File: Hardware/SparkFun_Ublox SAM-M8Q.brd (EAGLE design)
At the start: 40.6 x 40.6 mm, 74 parts, among them J13 Qwiic Right Angle, J3 PTH, J4 Qwiic Right Angle, U2 SAM-M8Q

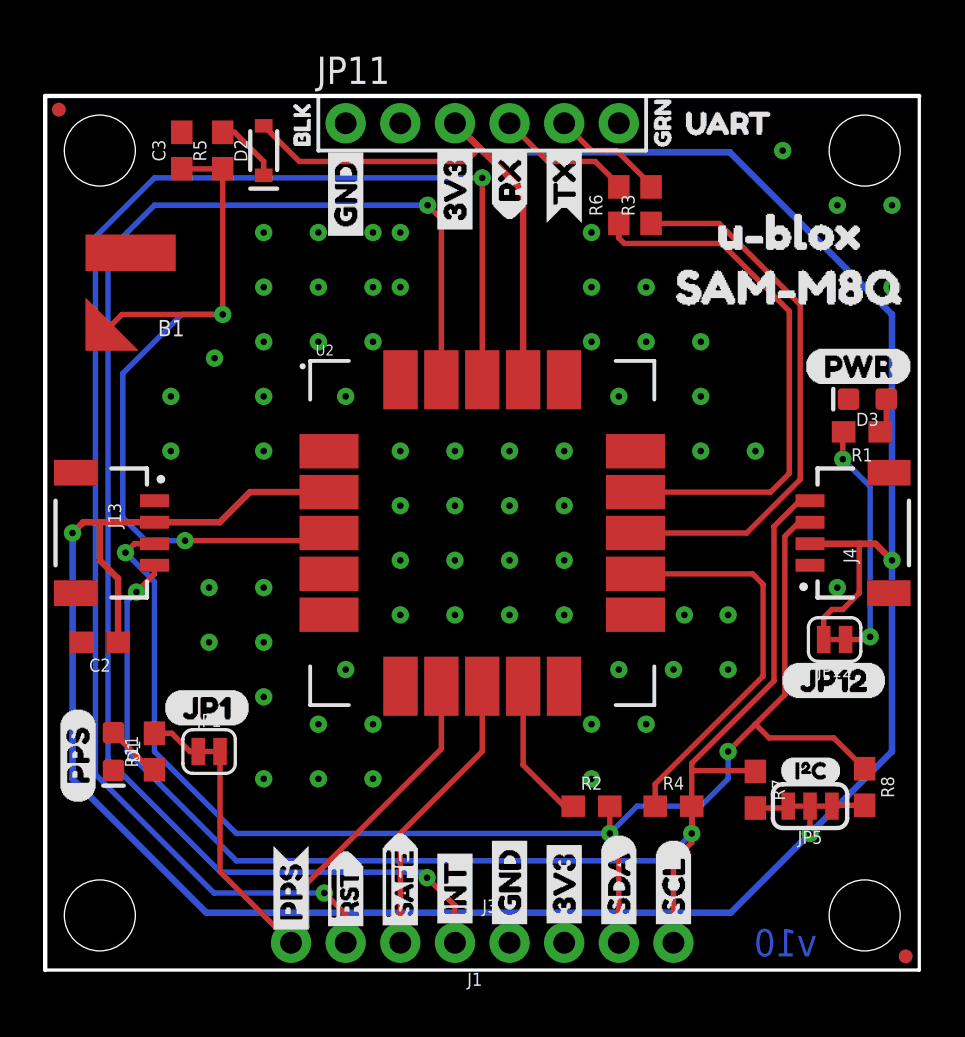
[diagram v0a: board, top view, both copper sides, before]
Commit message: Replaces all part with SparkFun parts, moves temp libarary parts to SparkFun Eagle libararies
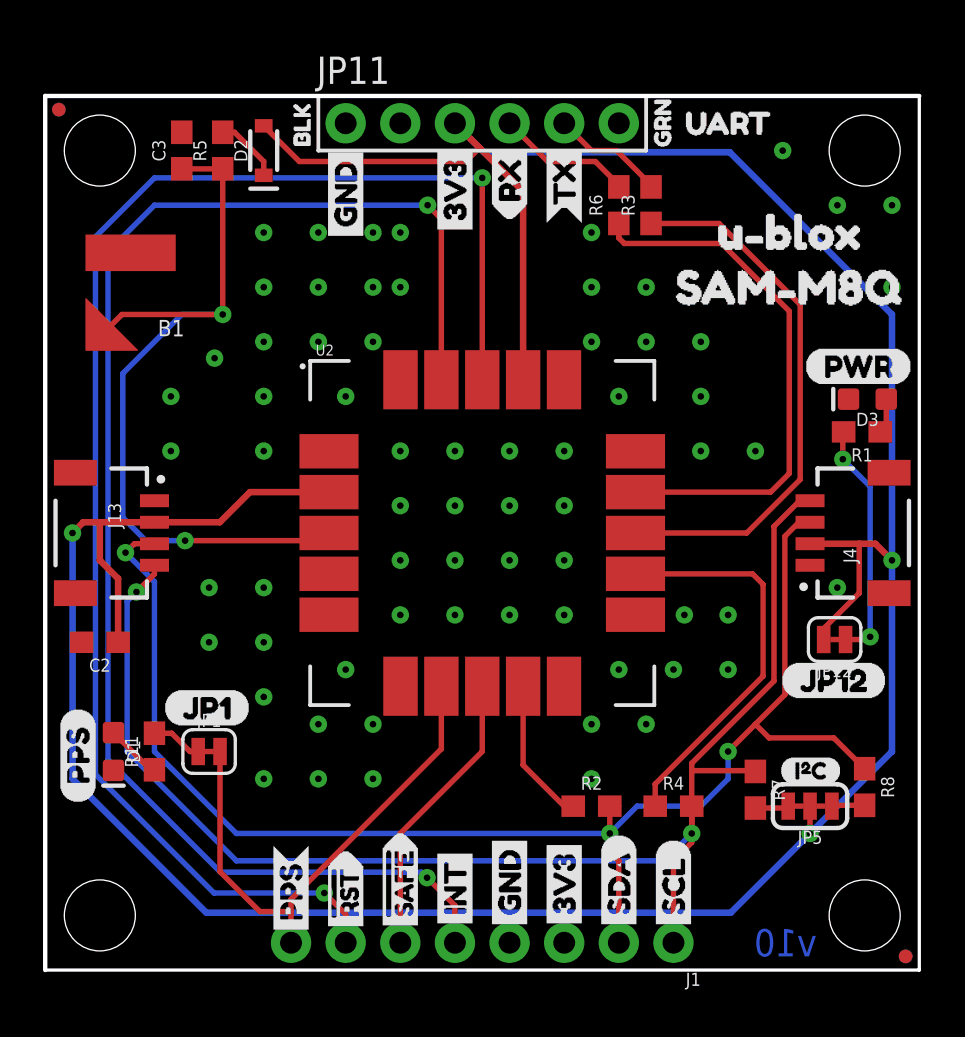
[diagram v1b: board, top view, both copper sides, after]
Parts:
- removed J3: PTH, SparkX:1X04_NO_SILK
- J1: device SparkFun-Connectors:1X04_NO_SILK -> SparkFun-Connectors:1X08_NO_SILK
- JP10, JP3, JP4, JP9: device SparkFun:STAND-OFF -> SparkFun-Hardware:STAND-OFF
- JP2, JP6, JP7, JP8: device SparkFun:MICRO-FIDUCIAL -> SparkFun-Aesthetics:FIDUCIAL-MICRO
- U2: value SAM-M8Q -> UBLOX_SAM-M8Q; device SAM-M8Q:SAM-M8Q -> SparkFun-GPS:SAM-M8Q
- moved J1 10.2 mm to (29.2, 1.27)
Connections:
- net !RESET: now also J1.7; no longer J1.3
- net !SAFE: now also J1.6; no longer J1.2
- net 3.3V: now also J1.3; no longer J3.2
- net GND: now also J1.4; no longer J3.1
- net INT: now also J1.5; no longer J1.1
- net PPS: now also J1.8; no longer J1.4
- net SCL: now also J1.1; no longer J3.4
- net SDA: now also J1.2; no longer J3.3
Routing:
- net PPS: track 25.1 -> 24.5 mm

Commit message: Changes all drill sizes to 15 mil, adjust schematic labels
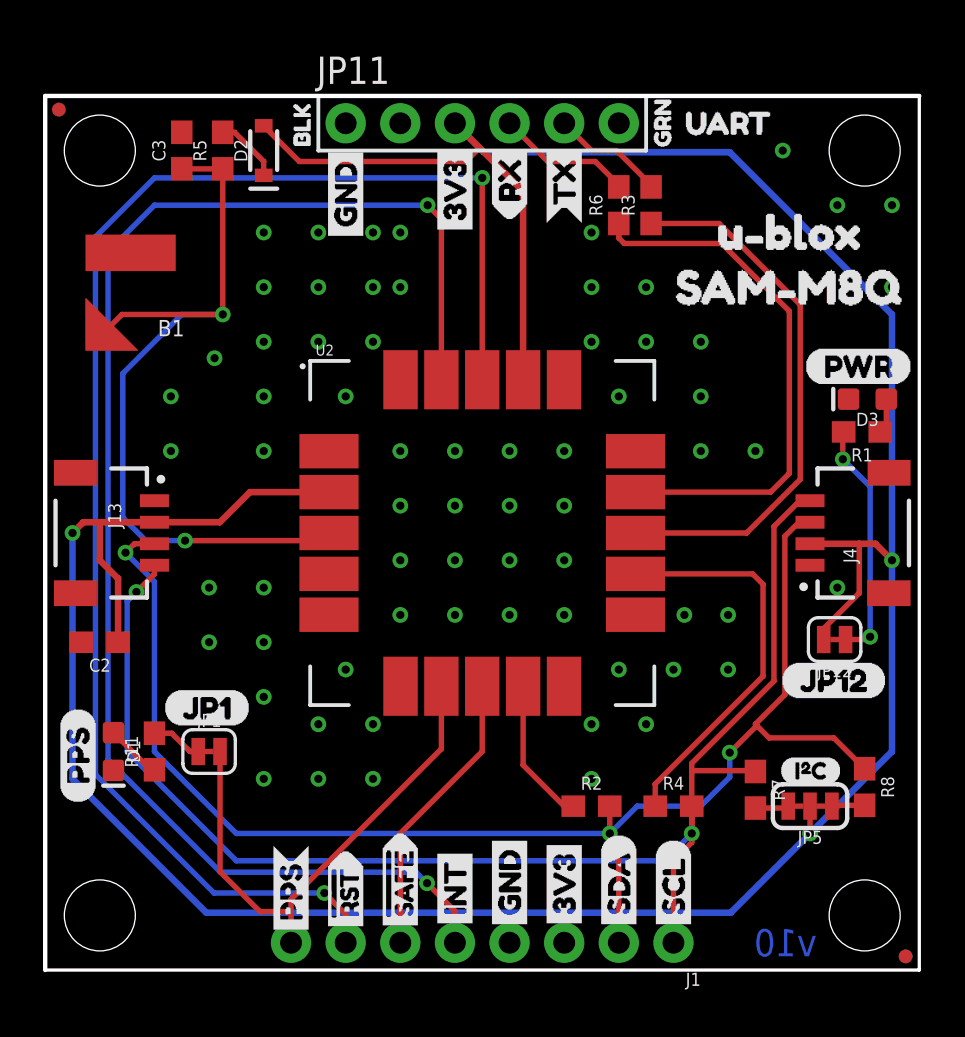
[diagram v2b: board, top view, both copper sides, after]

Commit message: Updates GPS module with updated part, adds VCC range and Battery text to schematic
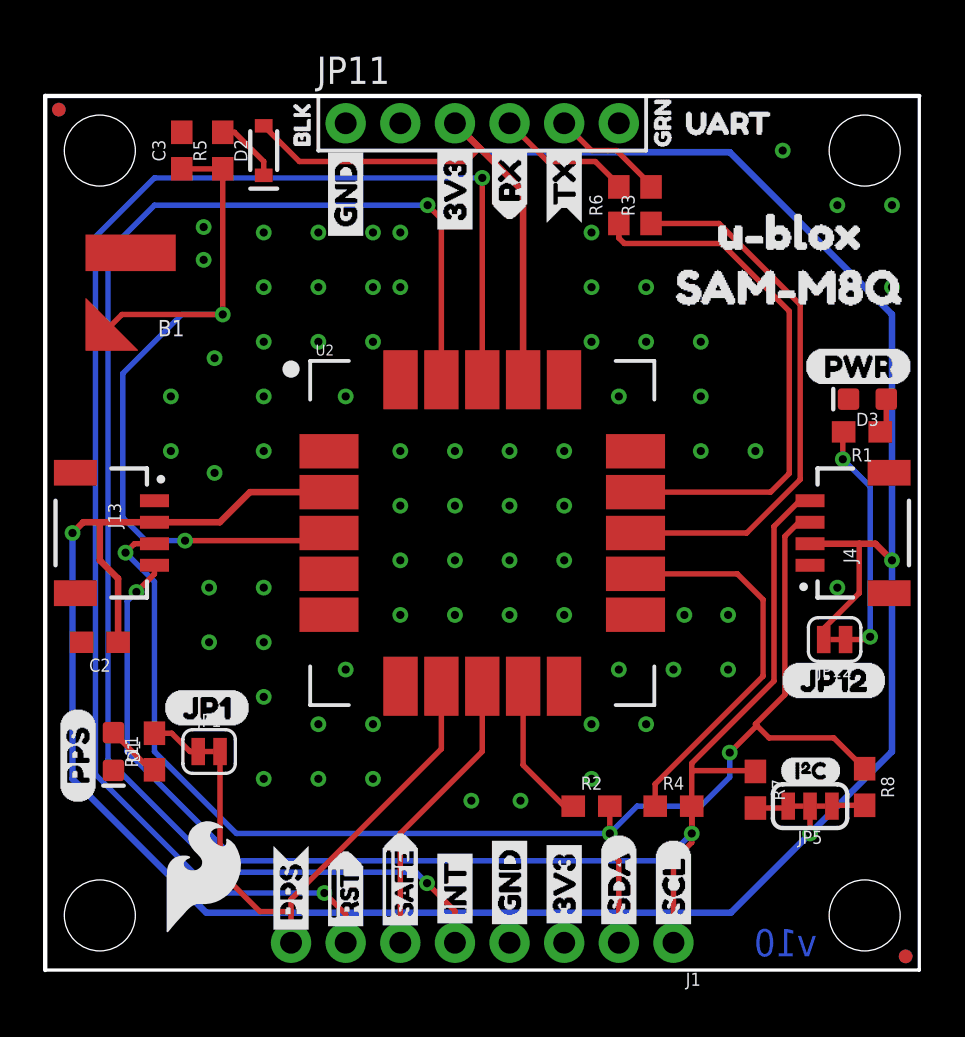
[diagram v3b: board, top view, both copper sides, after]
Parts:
- added U$2: (no value), SparkFun-Aesthetics:SFE_LOGO_FLAME_.2
- U2: value UBLOX_SAM-M8Q -> UBLOX_SAM_M8Q-0-10
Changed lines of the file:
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@@
 <?xml version="1.0" encoding="utf-8"?>
 <!DOCTYPE eagle SYSTEM "eagle.dtd">
-<eagle version="9.3.0">
+<eagle version="9.2.1">
 <drawing>
 <settings>
@@
 <element name="JP7" library="SparkFun-Aesthetics" package="FIDUCIAL-MICRO" value="FIDUCIALUFIDUCIAL" x="40.005" y="0.635" smashed="yes" rot="MR0"/>
 <element name="JP8" library="SparkFun-Aesthetics" package="FIDUCIAL-MICRO" value="FIDUCIALUFIDUCIAL" x="0.635" y="40.005" smashed="yes" rot="MR0"/>
-<element name="U2" library="SparkFun-GPS" package="SAM-M8Q" value="UBLOX_SAM-M8Q" x="20.32" y="20.32" smashed="yes">
+<element name="U2" library="SparkFun-GPS" package="SAM-M8Q" value="UBLOX_SAM_M8Q-0-10" x="20.32" y="20.32" smashed="yes">
 <attribute name="NAME" x="12.57" y="28.57" size="0.508" layer="25"/>
-<attribute name="PROD_ID" value="IC-14274" x="20.32" y="20.32" size="1.778" layer="27" display="off"/>
+<attribute name="PROD_ID" value="IC-14070" x="20.32" y="20.32" size="1.778" layer="27" display="off"/>
 <attribute name="VALUE" x="12.57" y="11.57" size="0.508" layer="27"/>
 </element>
@@
 <element name="U$28" library="JP12" package="JP120" value="" x="34.163" y="13.462" smashed="yes"/>
 <element name="U$30" library="PWR" package="PWR0" value="" x="35.306" y="28.067" smashed="yes"/>
+<element name="U$2" library="SparkFun-Aesthetics" package="SFE_LOGO_FLAME_.2" value="" x="7.366" y="4.318" smashed="yes"/>
 </elements>
 <signals>
@@
 <via x="7.874" y="28.448" extent="1-16" drill="0.381"/>
 <contactref element="J1" pad="4"/>
+<via x="7.366" y="34.544" extent="1-16" drill="0.381"/>
+<via x="7.366" y="33.02" extent="1-16" drill="0.381"/>
+<via x="22.098" y="7.874" extent="1-16" drill="0.381"/>
+<via x="19.812" y="7.874" extent="1-16" drill="0.381"/>
+<via x="7.874" y="23.114" extent="1-16" drill="0.381"/>
 </signal>
 <signal name="SCL">
@@
 <contactref element="U2" pad="12"/>
 <wire x1="28.36" y1="7.62" x2="28.36" y2="8.64885625" width="0.254" layer="1"/>
-<wire x1="32.888" y1="18.42" x2="33.3756" y2="17.9324" width="0.254" layer="1"/>
+<wire x1="32.1768" y1="18.42" x2="33.3756" y2="17.2212" width="0.254" layer="1"/>
 <wire x1="33.3756" y1="13.66445625" x2="28.36" y2="8.64885625" width="0.254" layer="1"/>
-<wire x1="27.445" y1="18.42" x2="32.888" y2="18.42" width="0.254" layer="1"/>
-<wire x1="33.3756" y1="17.9324" x2="33.3756" y2="13.66445625" width="0.254" layer="1"/>
+<wire x1="27.445" y1="18.42" x2="32.1768" y2="18.42" width="0.254" layer="1"/>
+<wire x1="33.3756" y1="17.2212" x2="33.3756" y2="13.66445625" width="0.254" layer="1"/>
 </signal>
 <signal name="!SAFE">

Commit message: Changes JP12 to JP2, fixes SDA trace, adds silk on top
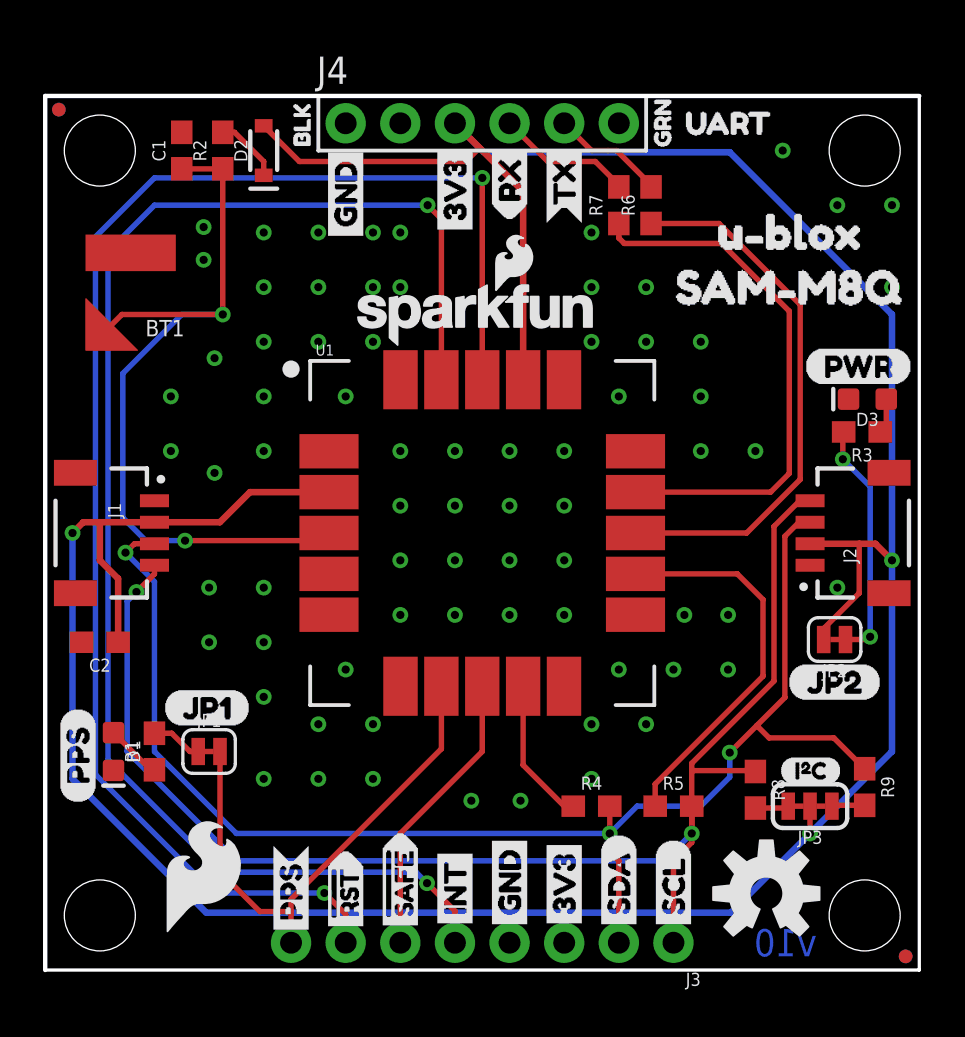
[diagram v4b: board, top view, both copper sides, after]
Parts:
- removed J13: Qwiic Right Angle, SparkFun-Connectors:JST04_1MM_RA
- removed JP11: BOOT, SparkFun-Connectors:1X06_NO_SILK
- removed JP12: JUMPER-SMT_2_NC_TRACE_SILK, SparkFun-Jumpers:SMT-JUMPER_2_NC_TRACE_SILK
- removed JP5: JUMPER-SMT_3_2-NC_TRACE_SILK, SparkFun-Jumpers:SMT-JUMPER_3_2-NC_TRACE_SILK
- removed JP6, JP7, JP8: FIDUCIALUFIDUCIAL, SparkFun-Aesthetics:FIDUCIAL-MICRO
- removed R11: 1k, SparkFun-Resistors:0603
- added FD1, FD2, FD3, FD4: FIDUCIALUFIDUCIAL, SparkFun-Aesthetics:FIDUCIAL-MICRO
- added H3: STAND-OFF, SparkFun-Hardware:STAND-OFF
- added J2: Qwiic Right Angle, SparkFun-Connectors:JST04_1MM_RA
- added J3: (no value), SparkFun-Connectors:1X08_NO_SILK
- added R9: 2.2k, SparkFun-Resistors:0603
- added U$31: (no value), JP2:JP20
- J1: value (none) -> Qwiic Right Angle; device SparkFun-Connectors:1X08_NO_SILK -> SparkFun-Connectors:JST04_1MM_RA
- J4: value Qwiic Right Angle -> BOOT; device SparkFun-Connectors:JST04_1MM_RA -> SparkFun-Connectors:1X06_NO_SILK
- JP2: value FIDUCIALUFIDUCIAL -> JUMPER-SMT_2_NC_TRACE_SILK; device SparkFun-Aesthetics:FIDUCIAL-MICRO -> SparkFun-Jumpers:SMT-JUMPER_2_NC_TRACE_SILK
- JP3: value STAND-OFF -> JUMPER-SMT_3_2-NC_TRACE_SILK; device SparkFun-Hardware:STAND-OFF -> SparkFun-Jumpers:SMT-JUMPER_3_2-NC_TRACE_SILK
- LOGO1: value OSHW-LOGOMINI -> SFE_LOGO_NAME_FLAME.2_INCH; device SparkFun-Aesthetics:OSHW-LOGO-MINI -> SparkFun-Aesthetics:SFE_LOGO_NAME_FLAME_.2
- LOGO2: value SFE_LOGO_NAME_FLAME.2_INCH -> OSHW-LOGOM; device SparkFun-Aesthetics:SFE_LOGO_NAME_FLAME_.2 -> SparkFun-Aesthetics:OSHW-LOGO-M
- R2: value 22 -> 3.3k
- R3: value 470 -> 1k
- R5: value 3.3k -> 22
- R7: value 2.2k -> 470
- U$28: device JP12:JP120 -> SparkFun-Aesthetics:SFE_LOGO_NAME_FLAME_.1
- moved JP3 44.9 mm to (35.6, 7.62), turned to 180 degrees
- moved R5 37.0 mm to (29.2, 7.62), turned to 0 degrees
- moved R1 36.1 mm to (5.08, 10.2), turned to 90 degrees
- moved R2 35.0 mm to (8.26, 38.1), turned to 90 degrees
- moved J1 30.7 mm to (5.08, 20.3), turned to 270 degrees
- moved J4 28.8 mm to (14.0, 39.4), turned to 0 degrees
- moved R7 27.9 mm to (26.7, 35.6), turned to 90 degrees
- moved U$28 22.1 mm to (20.1, 30.5)
- moved LOGO1 21.9 mm to (19.8, 19.8)
- moved LOGO2 21.3 mm to (33.5, 3.56), flipped to the top
- moved JP2 15.1 mm to (36.7, 15.4), turned to 180 degrees
- moved R3 14.4 mm to (38.0, 25.0), turned to 180 degrees
- moved R8 5.08 mm to (33.0, 8.38)
- moved R4 3.81 mm to (25.4, 7.62)
- moved R6 1.50 mm to (28.2, 35.6)
- renumbered B1 to BT1, C3 to C1, JP10 to H2, JP4 to H4, JP9 to H1, U2 to U1
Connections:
- net !RESET: now also J3.7; no longer J1.7
- net !SAFE: now also J3.6; no longer J1.6
- net 3.3V: now also J1.2, J2.2, J3.3, J4.3, JP2.2, JP3.2; no longer J1.3, J13.2, J4.2, JP11.3, JP12.2, JP5.2
- net BACKUP: now also R2.1; no longer R5.1
- net GND: now also J1.1, J2.1, J3.4, J4.2; no longer J1.4, J13.1, JP11.1, JP11.2
- net INT: now also J3.5; no longer J1.5
- net N$1: now also JP2.1, R3.2; no longer JP12.1, R1.2
- net N$2: now also R1.1; no longer R11.1
- net N$3: now also R3.1; no longer R1.1
- net N$4: now also R1.2; no longer R11.2
- net N$5: now also JP3.1, R9.2; no longer JP5.1, R8.2
- net N$6: now also R2.2; no longer R5.2
- net N$8: now also JP3.3, R8.2; no longer JP5.3, R7.2
- net PPS: now also J3.8; no longer J1.8
- net RXI: now also J4.4, R7.2; no longer JP11.4, R6.2
- net RXLV: now also R7.1; no longer R6.1
- net SCL: now also J1.4, J2.4, J3.1, R5.2, R8.1; no longer J1.1, J13.4, J4.4, R4.2, R7.1
- net SCL_LV: now also R5.1; no longer R4.1
- net SDA: now also J1.3, J2.3, J3.2, R4.2, R9.1; no longer J1.2, J13.3, J4.3, R2.2, R8.1
- net SDA_LV: now also R4.1; no longer R2.1
- net TXLV: now also R6.1; no longer R3.1
- net TXO: now also J4.5, R6.2; no longer JP11.5, R3.2

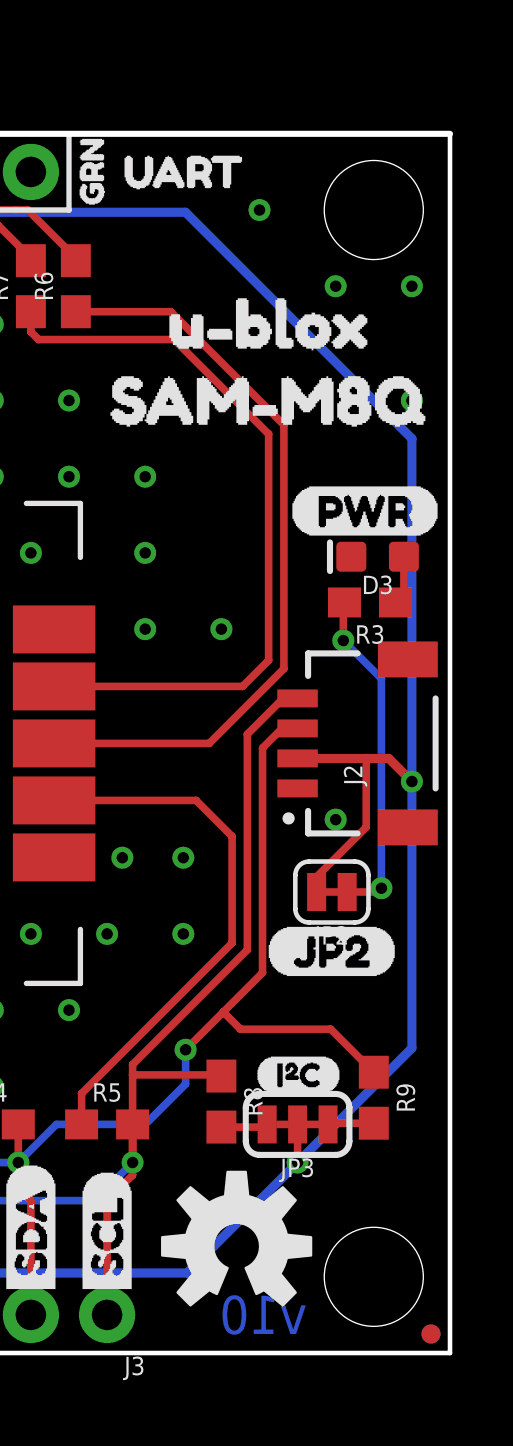
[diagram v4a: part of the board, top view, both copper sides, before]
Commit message: Changes polygon width to 10 mil and dimension to 8 mil
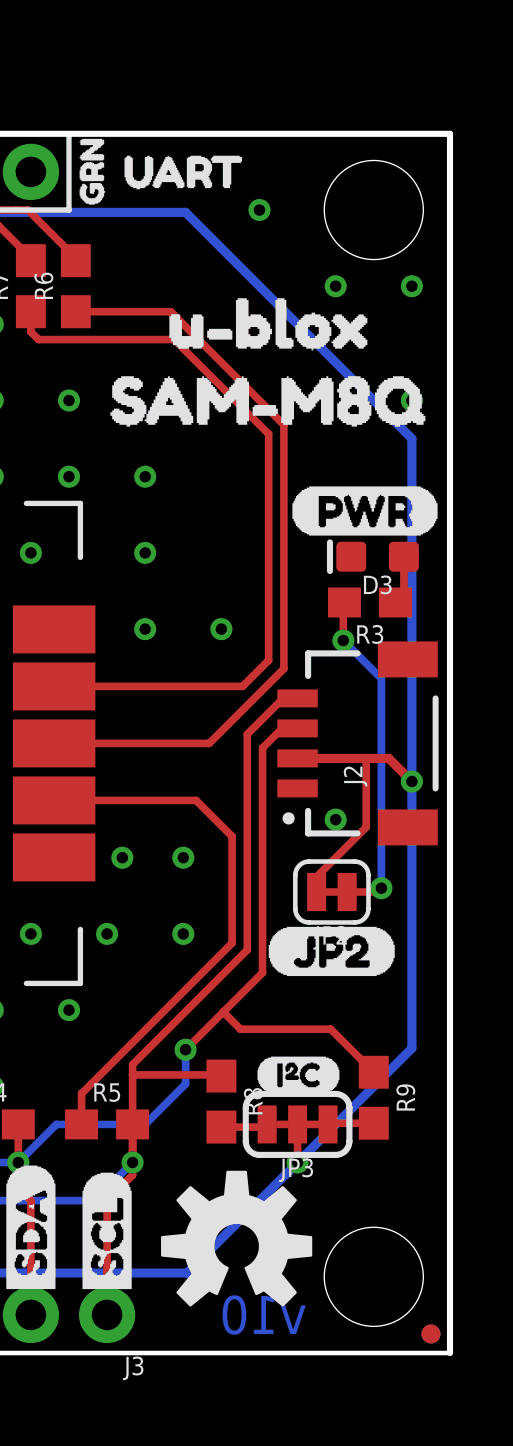
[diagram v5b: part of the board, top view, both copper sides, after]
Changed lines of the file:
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@@
 <wire x1="0" y1="0" x2="0" y2="40.64" width="0.2032" layer="20"/>
 <wire x1="0" y1="40.64" x2="40.64" y2="40.64" width="0.2032" layer="20"/>
-<wire x1="40.64" y1="40.64" x2="40.64" y2="0" width="0.1524" layer="20"/>
+<wire x1="40.64" y1="40.64" x2="40.64" y2="0" width="0.2032" layer="20"/>
 <wire x1="40.64" y1="0" x2="0" y2="0" width="0.1524" layer="20"/>
 <text x="34.417" y="1.27" size="1.27" layer="16" font="vector" ratio="15" rot="MR180" align="center">v10</text>
@@
 <contactref element="J4" pad="1"/>
 <contactref element="J4" pad="2"/>
-<polygon width="0.1524" layer="1" isolate="0.2032">
+<polygon width="0.254" layer="1" isolate="0.2032">
 <vertex x="0" y="40.64"/>
 <vertex x="40.64" y="40.64"/>
@@
 <vertex x="0" y="0"/>
 </polygon>
-<polygon width="0.1524" layer="16" isolate="0.2032">
+<polygon width="0.254" layer="16" isolate="0.2032">
 <vertex x="0" y="40.64"/>
 <vertex x="40.64" y="40.64"/>
@@
 <via x="19.812" y="7.874" extent="1-16" drill="0.381"/>
 <via x="7.874" y="23.114" extent="1-16" drill="0.381"/>
+<wire x1="37.35" y1="26.543" x2="33.02" y2="24.13" width="0" layer="19" extent="1-1"/>
 </signal>
 <signal name="SCL">
